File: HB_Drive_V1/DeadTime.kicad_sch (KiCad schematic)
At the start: 0 parts

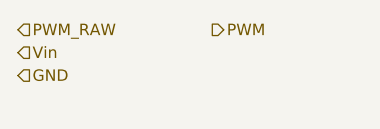
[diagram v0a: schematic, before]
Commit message: fixes git and adds a first revision of the Inner Current Regulator (NOT COMPLETE)
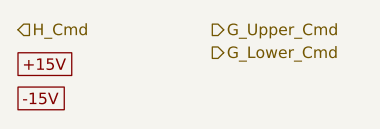
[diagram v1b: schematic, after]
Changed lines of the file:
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@@
 	(generator_version "10.0")
 	(paper "A4")
-	(hierarchical_label "PWM"
+	(global_label "-15V"
+		(shape passive)
+		(at 88.9 109.22 0)
+		(fields_autoplaced yes)
+		(effects
+			(font
+				(size 1.27 1.27)
+			)
+			(justify left)
+		)
+		(property "Intersheetrefs" "${INTERSHEET_REFS}"
+			(at 95.8539 109.22 0)
+			(hide yes)
+			(show_name no)
+			(do_not_autoplace no)
+			(effects
+				(font
+					(size 1.27 1.27)
+				)
+				(justify left)
+			)
+		)
+	)
+	(global_label "+15V"
+		(shape passive)
+		(at 88.9 105.41 0)
+		(fields_autoplaced yes)
+		(effects
+			(font
+				(size 1.27 1.27)
+			)
+			(justify left)
+		)
+		(property "Intersheetrefs" "${INTERSHEET_REFS}"
+			(at 95.8539 105.41 0)
+			(hide yes)
+			(show_name no)
+			(do_not_autoplace no)
+			(effects
+				(font
+					(size 1.27 1.27)
+				)
+				(justify left)
+			)
+		)
+	)
+	(hierarchical_label "G_Upper_Cmd"
 		(shape output)
 		(at 110.49 101.6 0)
@@
 		)
 	)
-	(hierarchical_label "Vin"
-		(shape input)
-		(at 88.9 104.14 0)
-		(effects
-			(font
-				(size 1.27 1.27)
-			)
-			(justify left)
-		)
-	)
-	(hierarchical_label "PWM_RAW"
+	(hierarchical_label "H_Cmd"
 		(shape input)
 		(at 88.9 101.6 0)
@@
 		)
 	)
-	(hierarchical_label "GND"
-		(shape input)
-		(at 88.9 106.68 0)
+	(hierarchical_label "G_Lower_Cmd"
+		(shape output)
+		(at 110.49 104.14 0)
 		(effects
 			(font

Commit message: Notes from conversation PF + MS
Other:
- note added: "Add deadtime circuit with 10 k potentiometer"
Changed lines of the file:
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@@
 	(generator_version "10.0")
 	(paper "A4")
+	(text "Add deadtime circuit with 10 k potentiometer"
+		(exclude_from_sim no)
+		(at 102.616 122.936 0)
+		(effects
+			(font
+				(size 1.27 1.27)
+			)
+		)
+	)
 	(global_label "-15V"
 		(shape passive)

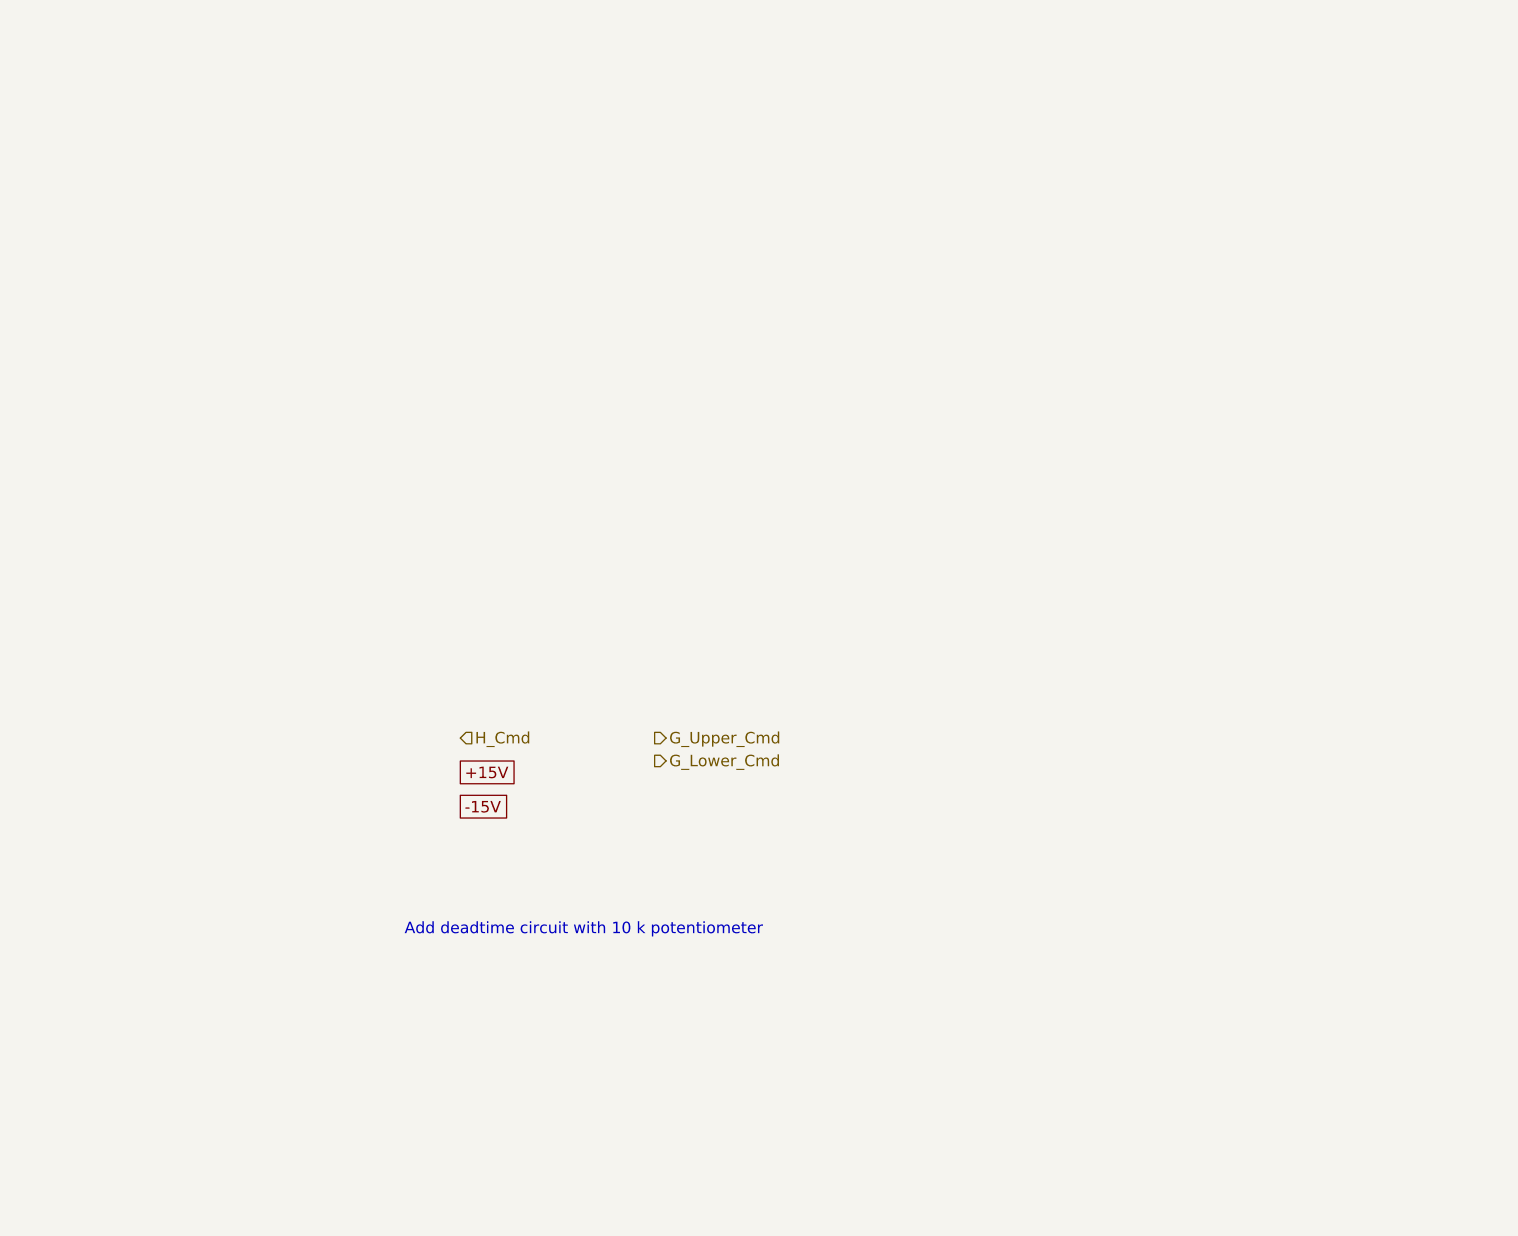
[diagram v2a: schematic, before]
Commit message: adds 10v reference and DC offsets / gain control to I_fdbk and V_fdbk
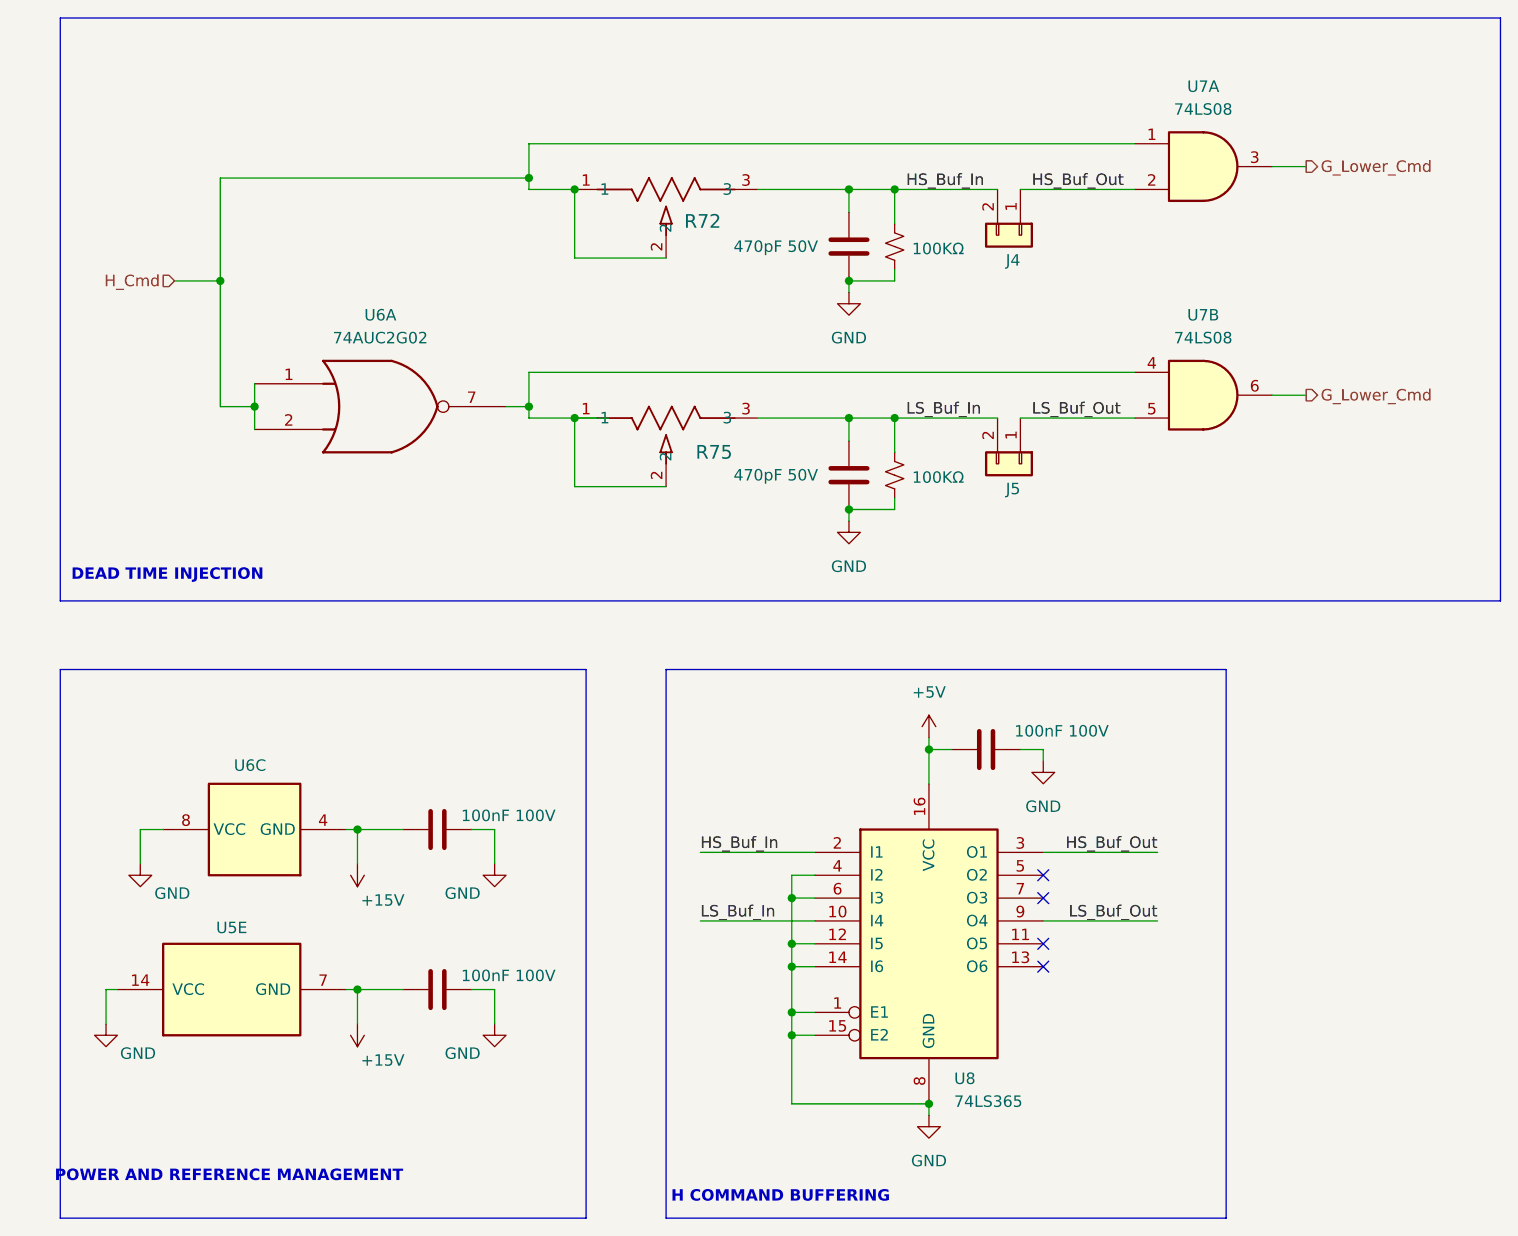
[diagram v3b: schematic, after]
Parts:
- added C12, C13: 470pF 50V, Capacitor_SMD:C_0603_1608Metric, symbol Device:C
- added C14, C40, C41: 100nF 100V, Capacitor_SMD:C_0603_1608Metric, symbol Device:C
- added J4, J5: Conn_01x02, Jumper:SolderJumper-2_P1.3mm_Open_TrianglePad1.0x1.5mm, symbol Connector_Generic:Conn_01x02
- added R30, R31: 100KΩ, Resistor_SMD:R_0603_1608Metric_Pad0.98x0.95mm_HandSolder, symbol Device:R_Small_US
- added R72, R75: PV36W502C01B00, POT_PV36W_BRN, symbol POT_PV36W_BRN:PV36W502C01B00
- added U5, U7: 74LS08, symbol 74xx:74LS08
- added U6: 74AUC2G02, symbol 74xGxx:74AUC2G02
- added U8: 74LS365, symbol 74xx:74LS365
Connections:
- net +15V: now also C40.2, C41.2, U5.7 (GND), U6.4 (GND)
- net G_Lower_Cmd: now also U7.3, U7.6
- net H_Cmd: now also R72.1, R72.2, U6.1, U6.2, U7.1
- new net: R75.1, R75.2, U6.7, U7.4
- new net +5V: C14.2, U8.16 (VCC)
- new net GND: C12.2, C13.2, C14.1, C40.1, C41.1, R30.2, R31.2, U5.14 (VCC), U6.8 (VCC), U8.1 (E1), U8.12 (I5), U8.14 (I6), U8.15 (E2), U8.4 (I2), U8.6 (I3), U8.8 (GND)
- new net HS_Buf_In: C12.1, J4.2 (Pin_2), R30.1, R72.3, U8.2 (I1)
- new net HS_Buf_Out: J4.1 (Pin_1), U7.2, U8.3 (O1)
- new net LS_Buf_In: C13.1, J5.2 (Pin_2), R31.1, R75.3, U8.10 (I4)
- new net LS_Buf_Out: J5.1 (Pin_1), U7.5, U8.9 (O4)
- no-connect marks 0 -> 4
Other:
- note added: "DEAD TIME INJECTION"
- note added: "H COMMAND BUFFERING"
- note added: "POWER AND REFERENCE MANAGEMENT"
- note removed: "Add deadtime circuit with 10 k potentiometer"
